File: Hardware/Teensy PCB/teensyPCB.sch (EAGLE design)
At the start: 27 parts, among them U2 USD-SOCKETNEW

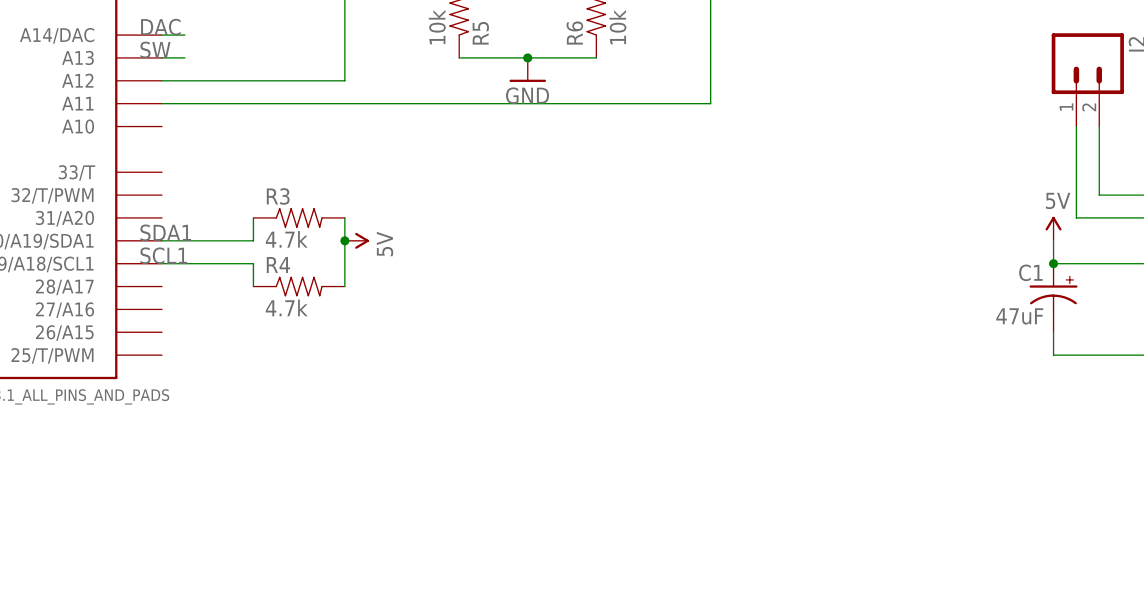
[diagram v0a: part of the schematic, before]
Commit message: Added "state" push buttons
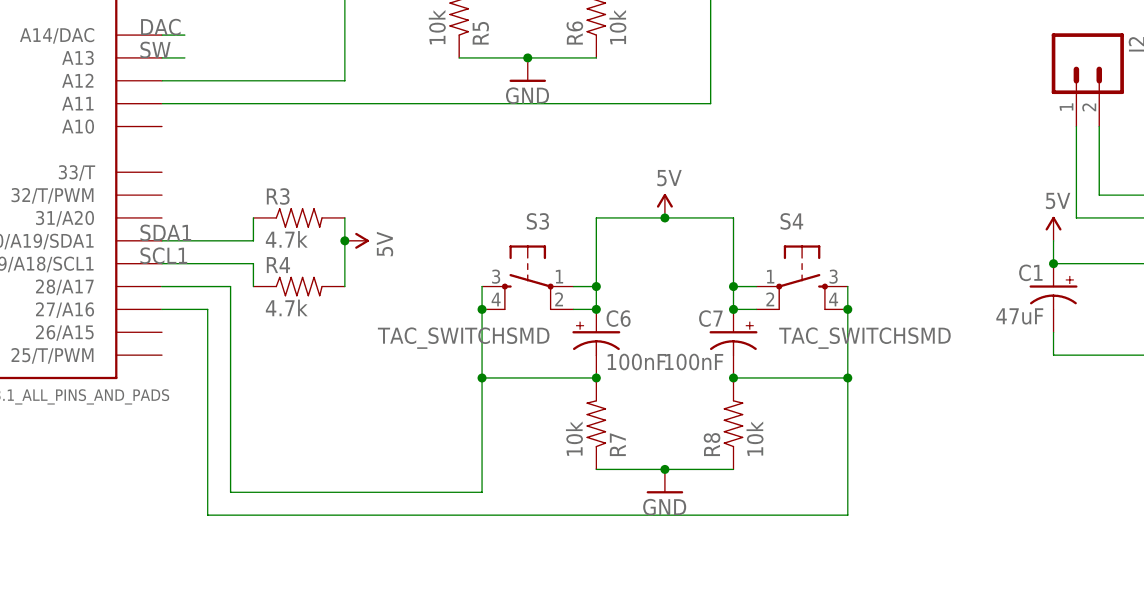
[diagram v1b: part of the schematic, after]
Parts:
- added C6, C7: 100nF, SparkFun-Capacitors:CAP_POL3528
- added R7, R8: 10k, SparkFun-Resistors:RESISTOR0805-RES
- added S3, S4: TAC_SWITCHSMD, SparkFun-Retired:TAC_SWITCHSMD
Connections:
- new net N$10: C7.-, R8.2, S4.3, S4.4, U$1.27/A16
- new net N$4: C6.-, R7.2, S3.3, S3.4, U$1.28/A17
- net 5V: now also C6.+, C7.+, S3.1, S3.2, S4.1, S4.2
- net GND: now also R7.1, R8.1
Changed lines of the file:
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@@
 <?xml version="1.0" encoding="utf-8"?>
 <!DOCTYPE eagle SYSTEM "eagle.dtd">
-<eagle version="7.5.0">
+<eagle version="7.2.0">
 <drawing>
 <settings>
@@
 <part name="BAT1" library="SparkFun-Electromechanical" deviceset="BATTERY" device="20PTH"/>
 <part name="GND10" library="SparkFun-Aesthetics" deviceset="GND" device=""/>
+<part name="S3" library="SparkFun-Retired" deviceset="TAC_SWITCH" device="SMD" value="TAC_SWITCHSMD"/>
+<part name="R7" library="SparkFun-Resistors" deviceset="RESISTOR" device="0805-RES" value="10k"/>
+<part name="C6" library="SparkFun-Capacitors" deviceset="CAP_POL" device="3528" value="100nF"/>
+<part name="S4" library="SparkFun-Retired" deviceset="TAC_SWITCH" device="SMD" value="TAC_SWITCHSMD"/>
+<part name="R8" library="SparkFun-Resistors" deviceset="RESISTOR" device="0805-RES" value="10k"/>
+<part name="C7" library="SparkFun-Capacitors" deviceset="CAP_POL" device="3528" value="100nF"/>
+<part name="SUPPLY7" library="SparkFun-Aesthetics" deviceset="5V" device=""/>
+<part name="GND11" library="SparkFun-Aesthetics" deviceset="GND" device=""/>
 </parts>
 <sheets>
@@
 <instance part="BAT1" gate="G$1" x="58.42" y="53.34" rot="R270"/>
 <instance part="GND10" gate="1" x="58.42" y="45.72"/>
+<instance part="S3" gate="S" x="81.28" y="-15.24" rot="MR0"/>
+<instance part="R7" gate="G$1" x="88.9" y="-30.48" rot="MR90"/>
+<instance part="C6" gate="G$1" x="88.9" y="-20.32"/>
+<instance part="S4" gate="S" x="111.76" y="-15.24"/>
+<instance part="R8" gate="G$1" x="104.14" y="-30.48" rot="R90"/>
+<instance part="C7" gate="G$1" x="104.14" y="-20.32" rot="MR0"/>
+<instance part="SUPPLY7" gate="G$1" x="96.52" y="-7.62"/>
+<instance part="GND11" gate="1" x="96.52" y="-38.1"/>
 </instances>
 <busses>
@@
 <pinref part="BAT1" gate="G$1" pin="-"/>
 <pinref part="GND10" gate="1" pin="GND"/>
+</segment>
+<segment>
+<pinref part="R7" gate="G$1" pin="1"/>
+<pinref part="R8" gate="G$1" pin="1"/>
+<wire x1="88.9" y1="-35.56" x2="96.52" y2="-35.56" width="0.1524" layer="91"/>
+<pinref part="GND11" gate="1" pin="GND"/>
+<wire x1="96.52" y1="-35.56" x2="104.14" y2="-35.56" width="0.1524" layer="91"/>
+<junction x="96.52" y="-35.56"/>
 </segment>
 </net>
@@
 <pinref part="SUPPLY15" gate="G$1" pin="5V"/>
 </segment>
+<segment>
+<pinref part="C6" gate="G$1" pin="+"/>
+<pinref part="S3" gate="S" pin="2"/>
+<wire x1="86.36" y1="-17.78" x2="88.9" y2="-17.78" width="0.1524" layer="91"/>
+<pinref part="S3" gate="S" pin="1"/>
+<wire x1="86.36" y1="-15.24" x2="88.9" y2="-15.24" width="0.1524" layer="91"/>
+<wire x1="88.9" y1="-15.24" x2="88.9" y2="-17.78" width="0.1524" layer="91"/>
+<junction x="88.9" y="-17.78"/>
+<wire x1="88.9" y1="-15.24" x2="88.9" y2="-7.62" width="0.1524" layer="91"/>
+<junction x="88.9" y="-15.24"/>
+<pinref part="C7" gate="G$1" pin="+"/>
+<pinref part="S4" gate="S" pin="2"/>
+<wire x1="106.68" y1="-17.78" x2="104.14" y2="-17.78" width="0.1524" layer="91"/>
+<pinref part="S4" gate="S" pin="1"/>
+<wire x1="106.68" y1="-15.24" x2="104.14" y2="-15.24" width="0.1524" layer="91"/>
+<wire x1="104.14" y1="-15.24" x2="104.14" y2="-17.78" width="0.1524" layer="91"/>
+<junction x="104.14" y="-17.78"/>
+<wire x1="104.14" y1="-15.24" x2="104.14" y2="-7.62" width="0.1524" layer="91"/>
+<junction x="104.14" y="-15.24"/>
+<wire x1="104.14" y1="-7.62" x2="96.52" y2="-7.62" width="0.1524" layer="91"/>
+<pinref part="SUPPLY7" gate="G$1" pin="5V"/>
+<wire x1="96.52" y1="-7.62" x2="88.9" y2="-7.62" width="0.1524" layer="91"/>
+<junction x="96.52" y="-7.62"/>
+</segment>
 </net>
 <net name="ARDUINO_RX" class="0">
@@
 </segment>
 </net>
+<net name="N$4" class="0">
+<segment>
+<pinref part="S3" gate="S" pin="4"/>
+<pinref part="S3" gate="S" pin="3"/>
+<wire x1="76.2" y1="-15.24" x2="76.2" y2="-17.78" width="0.1524" layer="91"/>
+<junction x="76.2" y="-17.78"/>
+<pinref part="R7" gate="G$1" pin="2"/>
+<pinref part="C6" gate="G$1" pin="-"/>
+<junction x="88.9" y="-25.4"/>
+<wire x1="88.9" y1="-25.4" x2="76.2" y2="-25.4" width="0.1524" layer="91"/>
+<wire x1="76.2" y1="-25.4" x2="76.2" y2="-17.78" width="0.1524" layer="91"/>
+<wire x1="48.26" y1="-38.1" x2="76.2" y2="-38.1" width="0.1524" layer="91"/>
+<wire x1="76.2" y1="-38.1" x2="76.2" y2="-25.4" width="0.1524" layer="91"/>
+<junction x="76.2" y="-25.4"/>
+<pinref part="U$1" gate="G$1" pin="28/A17"/>
+<wire x1="40.64" y1="-15.24" x2="48.26" y2="-15.24" width="0.1524" layer="91"/>
+<wire x1="48.26" y1="-15.24" x2="48.26" y2="-38.1" width="0.1524" layer="91"/>
+</segment>
+</net>
+<net name="N$10" class="0">
+<segment>
+<pinref part="S4" gate="S" pin="4"/>
+<pinref part="S4" gate="S" pin="3"/>
+<wire x1="116.84" y1="-15.24" x2="116.84" y2="-17.78" width="0.1524" layer="91"/>
+<junction x="116.84" y="-17.78"/>
+<pinref part="R8" gate="G$1" pin="2"/>
+<pinref part="C7" gate="G$1" pin="-"/>
+<junction x="104.14" y="-25.4"/>
+<wire x1="104.14" y1="-25.4" x2="116.84" y2="-25.4" width="0.1524" layer="91"/>
+<wire x1="116.84" y1="-25.4" x2="116.84" y2="-17.78" width="0.1524" layer="91"/>
+<wire x1="116.84" y1="-40.64" x2="116.84" y2="-25.4" width="0.1524" layer="91"/>
+<junction x="116.84" y="-25.4"/>
+<wire x1="45.72" y1="-40.64" x2="116.84" y2="-40.64" width="0.1524" layer="91"/>
+<pinref part="U$1" gate="G$1" pin="27/A16"/>
+<wire x1="40.64" y1="-17.78" x2="45.72" y2="-17.78" width="0.1524" layer="91"/>
+<wire x1="45.72" y1="-17.78" x2="45.72" y2="-40.64" width="0.1524" layer="91"/>
+</segment>
+</net>

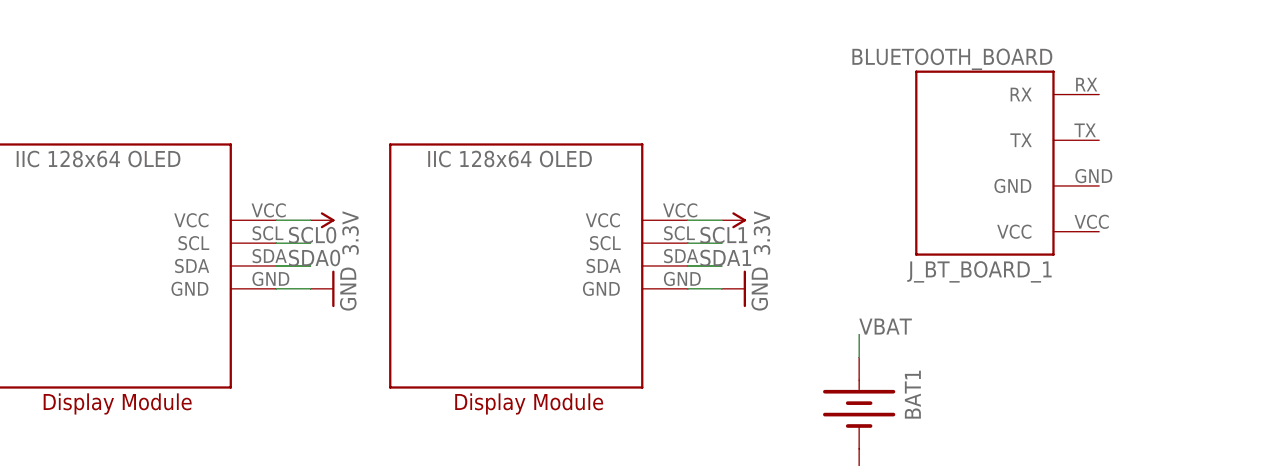
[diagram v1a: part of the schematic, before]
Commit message: Updated hole spacing and layout
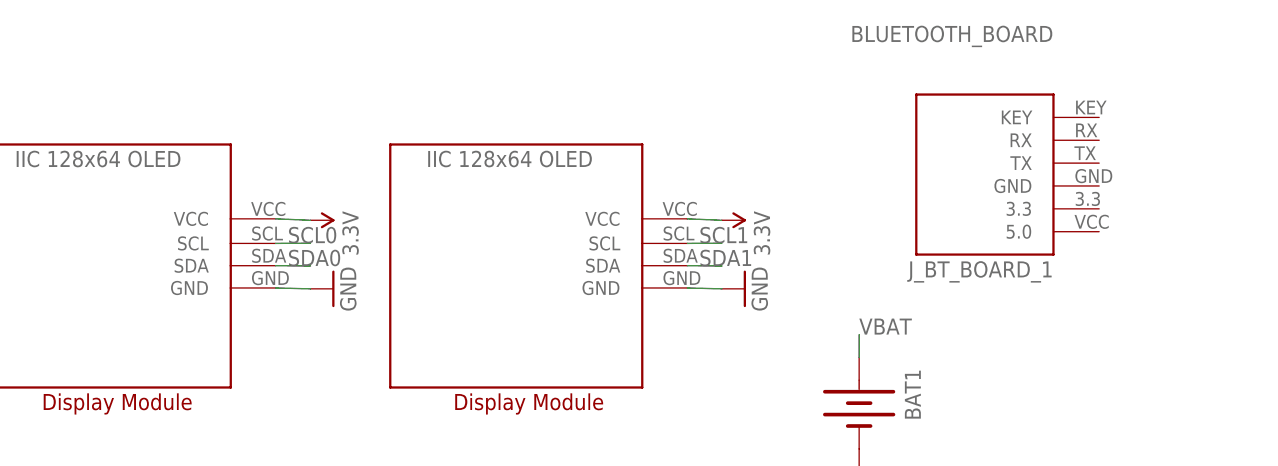
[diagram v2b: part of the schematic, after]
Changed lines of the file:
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@@
 <segment>
 <pinref part="U$2" gate="G$1" pin="GND"/>
-<wire x1="-2.54" y1="66.04" x2="-6.35" y2="66.04" width="0.1524" layer="91"/>
+<wire x1="-2.54" y1="66.04" x2="-6.4" y2="66.136" width="0.1524" layer="91"/>
 <pinref part="GND5" gate="1" pin="GND"/>
 </segment>
 <segment>
 <pinref part="U$3" gate="G$1" pin="GND"/>
-<wire x1="43.18" y1="66.04" x2="39.37" y2="66.04" width="0.1524" layer="91"/>
+<wire x1="43.18" y1="66.04" x2="39.32" y2="66.136" width="0.1524" layer="91"/>
 <pinref part="GND6" gate="1" pin="GND"/>
 </segment>
@@
 <segment>
 <pinref part="U$2" gate="G$1" pin="VCC"/>
-<wire x1="-2.54" y1="73.66" x2="-6.35" y2="73.66" width="0.1524" layer="91"/>
+<wire x1="-2.54" y1="73.66" x2="-6.4" y2="73.818" width="0.1524" layer="91"/>
 <pinref part="SUPPLY5" gate="G$1" pin="3.3V"/>
 </segment>
 <segment>
 <pinref part="U$3" gate="G$1" pin="VCC"/>
-<wire x1="43.18" y1="73.66" x2="39.37" y2="73.66" width="0.1524" layer="91"/>
+<wire x1="43.18" y1="73.66" x2="39.32" y2="73.818" width="0.1524" layer="91"/>
 <pinref part="SUPPLY6" gate="G$1" pin="3.3V"/>
 </segment>
@@
 <segment>
 <pinref part="U$2" gate="G$1" pin="SDA"/>
-<wire x1="-2.54" y1="68.58" x2="-6.35" y2="68.58" width="0.1524" layer="91"/>
+<wire x1="-2.54" y1="68.58" x2="-6.4" y2="68.612" width="0.1524" layer="91"/>
 <label x="-5.08" y="68.58" size="1.778" layer="95"/>
 </segment>
@@
 <segment>
 <pinref part="U$2" gate="G$1" pin="SCL"/>
-<wire x1="-2.54" y1="71.12" x2="-6.35" y2="71.12" width="0.1524" layer="91"/>
+<wire x1="-2.54" y1="71.12" x2="-6.4" y2="71.088" width="0.1524" layer="91"/>
 <label x="-5.08" y="71.12" size="1.778" layer="95"/>
 </segment>
@@
 <segment>
 <pinref part="U$3" gate="G$1" pin="SDA"/>
-<wire x1="43.18" y1="68.58" x2="39.37" y2="68.58" width="0.1524" layer="91"/>
+<wire x1="43.18" y1="68.58" x2="39.32" y2="68.612" width="0.1524" layer="91"/>
 <label x="40.64" y="68.58" size="1.778" layer="95"/>
 </segment>
@@
 <segment>
 <pinref part="U$3" gate="G$1" pin="SCL"/>
-<wire x1="43.18" y1="71.12" x2="39.37" y2="71.12" width="0.1524" layer="91"/>
+<wire x1="43.18" y1="71.12" x2="39.32" y2="71.088" width="0.1524" layer="91"/>
 <label x="40.64" y="71.12" size="1.778" layer="95"/>
 </segment>

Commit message: layout work
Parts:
- removed R1, R2, R3, R4: 4.7k, SparkFun-Resistors:RESISTOR0805-RES
- C3, C4, C6, C7: value 100nF -> 1.0uF; device SparkFun-Capacitors:CAP_POL3528 -> SparkFun-Capacitors:1.0UF-25V-+80/-20(0805)
- S1: value TAC_SWITCHSMD -> UP
- S2: value TAC_SWITCHSMD -> DOWN
- S3: value TAC_SWITCHSMD -> LEFT
- S4: value TAC_SWITCHSMD -> RIGHT
- U$4: value AUDIOAMP -> AUDIOAMPEBAY_VERSION; device CLASS D AUDIO AMP:AUDIOAMP -> CLASS D AUDIO AMP:AUDIOAMPEBAY_VERSION
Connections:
- net 5V: now also C3.1, C4.1, C6.1, C7.1; no longer C3.+, C4.+, C6.+, C7.+, R1.2, R2.2, R3.2, R4.2
- net GND: now also U$4.AGND, U$4.GND; no longer U$4.GND0, U$4.GND1, U$4.GND2
- net N$10: now also C4.2; no longer C7.-
- net N$2: now also C7.2; no longer C4.-
- net N$4: now also C3.2; no longer C6.-
- net N$9: now also C6.2; no longer C3.-
- net SCL0: no longer R2.1
- net SCL1: no longer R4.1
- net SDA0: no longer R1.1
- net SDA1: no longer R3.1
- net SW: no longer U$4.SW
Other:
- moved on the sheet: C2

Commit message: more layout
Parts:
- added C8: 10uF, SparkFun-Capacitors:1.0UF-25V-+80/-20(0805)
- added C9: 1uF, SparkFun-Capacitors:1.0UF-25V-+80/-20(0805)
- C2: device SparkFun-Capacitors:CAP_POL3528 -> SparkFun-Capacitors:1.0UF-25V-+80/-20(0805)
- C5: value 10uF -> 47uF
- renumbered J_ULTRASONIC_1 to USONIC2, J_ULTRASONIC_2 to USONIC1, LINEAR_ARRAY_SENSOR2 to LIN_ARRAY
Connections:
- net 3.3V: now also C5.+, C9.1
- net DAC: now also C8.2; no longer C5.+
- net GND: now also C5.-, C9.2
- net N$1: now also C2.1; no longer C2.-
- net N$3: now also C8.1; no longer C5.-
- net WOUT: now also C2.2; no longer C2.+
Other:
- moved on the sheet: C5
